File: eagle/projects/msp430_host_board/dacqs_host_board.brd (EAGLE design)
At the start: 127 x 100 mm, 271 parts, among them J1 MOL-SL-4-RA, J10 MOL-SL-3-V, J11 MOL-SL-2-V, J12 CONN HEADER 20POS .100" DBL, J13 MOL-SL-2-RA, J14 USB_MICROB_RECPT, J16 MOL-SL-2-RA, J17 CLM-112-02-L-D-IMU-MOUNT_IMU, J18 MOLSL-7-RA, J19 CONN HEADER 20POS .100" DBL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

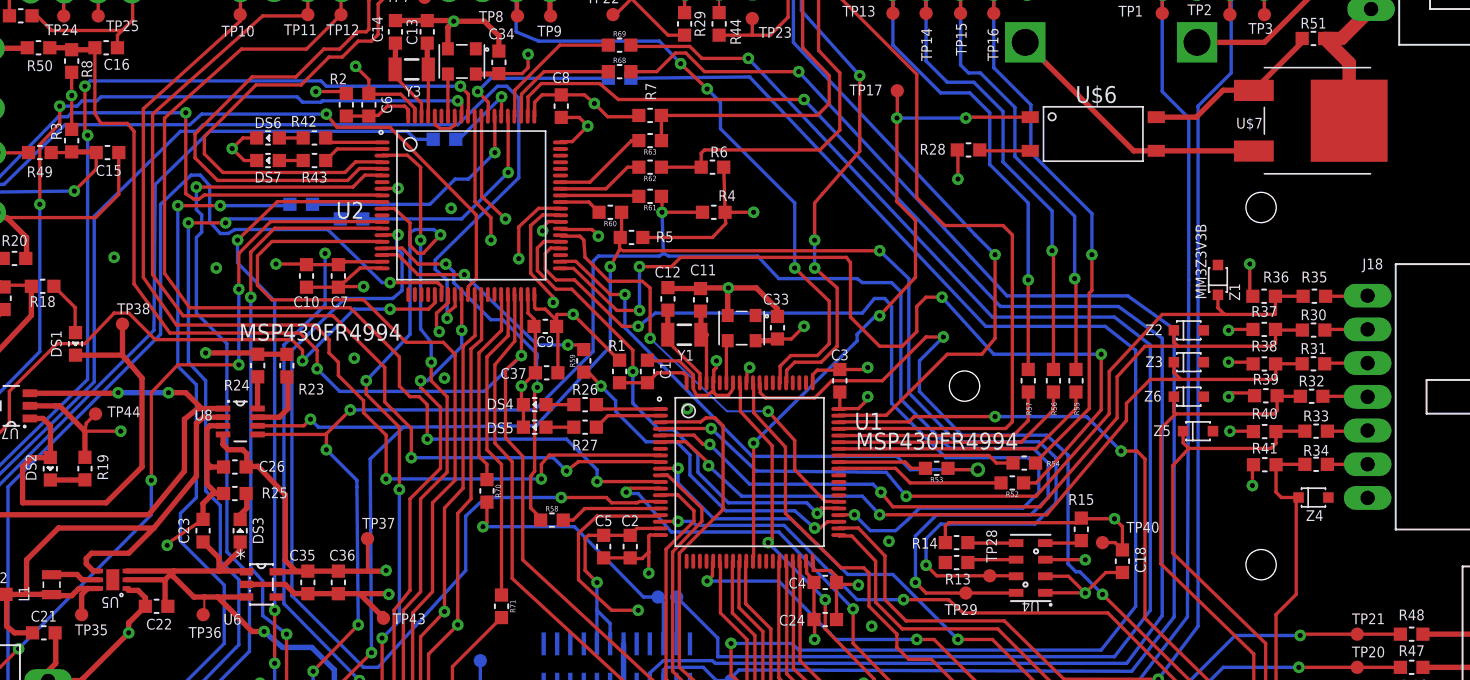
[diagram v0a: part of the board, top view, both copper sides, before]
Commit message: Small fixes to power packages and power fet layout
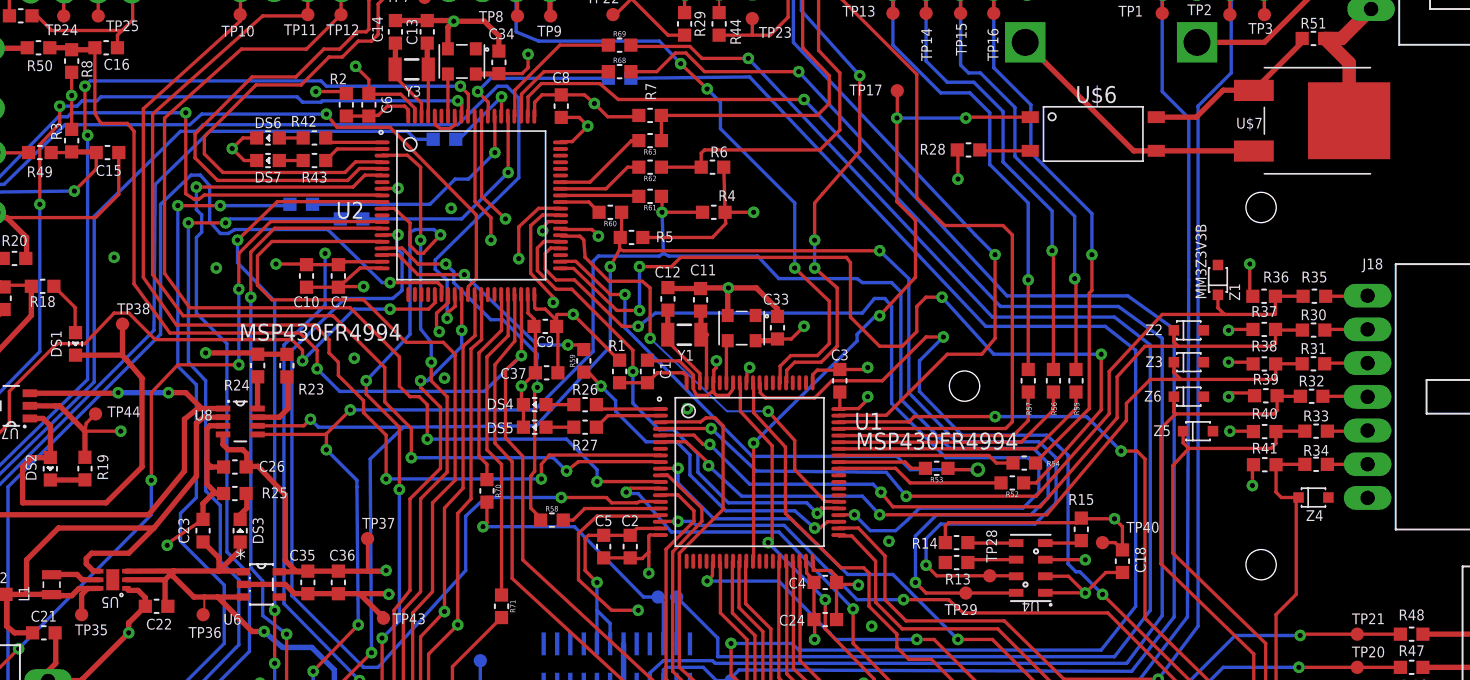
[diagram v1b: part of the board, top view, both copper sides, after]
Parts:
- R49, R50: value 47k -> 49.9
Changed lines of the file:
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@@
 <attribute name="VALUE" x="116.4" y="38.55" size="0.254" layer="27" ratio="6" rot="R180" align="center"/>
 </element>
-<element name="R49" library="daqcs_host" package="R0603" value="47k" x="13" y="74.1" smashed="yes">
-<attribute name="MANUFACTURER_PN" value="ERJ-3EKF4702V" x="13" y="74.1" size="1.778" layer="27" display="off"/>
+<element name="R49" library="daqcs_host" package="R0603" value="49.9" x="13" y="74.1" smashed="yes">
+<attribute name="MANUFACTURER_PN" value="ERJ-3EKF49R9V" x="13" y="74.1" size="1.778" layer="27" display="off"/>
 <attribute name="TOLERANCE" value="1%" x="13" y="74.1" size="1.778" layer="27" display="off"/>
-<attribute name="VENDOR_PN" value="P47.0KHCT-ND" x="13" y="74.1" size="1.778" layer="27" display="off"/>
+<attribute name="VENDOR_PN" value="P49.9HCT-ND" x="13" y="74.1" size="1.778" layer="27" display="off"/>
 <attribute name="MANUFACTURER" value="Panasonic" x="13" y="74.1" size="1.778" layer="27" display="off"/>
 <attribute name="POWER" value="1/10W" x="13" y="74.1" size="1.778" layer="27" display="off"/>
 <attribute name="VENDOR" value="Digi-key" x="13" y="74.1" size="1.778" layer="27" display="off"/>
 <attribute name="NAME" x="13" y="72.65" size="0.8128" layer="25" ratio="15" align="center"/>
-<attribute name="VALUE" x="13" y="73.35" size="0.254" layer="27" ratio="6" align="center"/>
+<attribute name="VALUE" value="49.9" x="13" y="73.35" size="0.254" layer="27" ratio="6" align="center"/>
 </element>
-<element name="R50" library="daqcs_host" package="R0603" value="47k" x="12.9" y="82" smashed="yes">
-<attribute name="MANUFACTURER_PN" value="ERJ-3EKF4702V" x="12.9" y="82" size="1.778" layer="27" display="off"/>
+<element name="R50" library="daqcs_host" package="R0603" value="49.9" x="12.9" y="82" smashed="yes">
+<attribute name="MANUFACTURER_PN" value="ERJ-3EKF49R9V" x="12.9" y="82" size="1.778" layer="27" display="off"/>
 <attribute name="TOLERANCE" value="1%" x="12.9" y="82" size="1.778" layer="27" display="off"/>
-<attribute name="VENDOR_PN" value="P47.0KHCT-ND" x="12.9" y="82" size="1.778" layer="27" display="off"/>
+<attribute name="VENDOR_PN" value="P49.9HCT-ND" x="12.9" y="82" size="1.778" layer="27" display="off"/>
 <attribute name="MANUFACTURER" value="Panasonic" x="12.9" y="82" size="1.778" layer="27" display="off"/>
 <attribute name="POWER" value="1/10W" x="12.9" y="82" size="1.778" layer="27" display="off"/>
 <attribute name="VENDOR" value="Digi-key" x="12.9" y="82" size="1.778" layer="27" display="off"/>
 <attribute name="NAME" x="13" y="80.65" size="0.8128" layer="25" ratio="15" align="center"/>
-<attribute name="VALUE" x="12.9" y="81.25" size="0.254" layer="27" ratio="6" align="center"/>
+<attribute name="VALUE" value="49.9" x="12.9" y="81.25" size="0.254" layer="27" ratio="6" align="center"/>
 </element>
 <element name="TP39" library="daqcs_host" package="TP10R" value="" x="32.4" y="21.2" smashed="yes">
@@
 <wire x1="31.5" y1="48.3" x2="31.5" y2="43.35" width="0.4064" layer="1"/>
 <wire x1="31.5" y1="43.35" x2="32.3" y2="42.55" width="0.4064" layer="1"/>
-<wire x1="30.8176" y1="42.5" x2="33.15" y2="42.5" width="0.4064" layer="1"/>
+<wire x1="31.05" y1="42.5" x2="33.15" y2="42.5" width="0.4064" layer="1"/>
 <wire x1="33.15" y1="42.5" x2="33.2" y2="42.55" width="0.4064" layer="1"/>
 <wire x1="37.7" y1="42.55" x2="39.05" y2="42.55" width="0.4064" layer="1"/>
@@
 <wire x1="38.9" y1="39.34290625" x2="38.60709375" y2="39.34290625" width="0.4064" layer="1"/>
 <wire x1="38.60709375" y1="39.34290625" x2="37.1" y2="40.85" width="0.4064" layer="1"/>
-<wire x1="28.5824" y1="41.55" x2="31.5" y2="41.55" width="0.4064" layer="1"/>
+<wire x1="28.35" y1="41.55" x2="31.5" y2="41.55" width="0.4064" layer="1"/>
 <wire x1="31.5" y1="41.55" x2="32.2" y2="40.85" width="0.4064" layer="1"/>
 <wire x1="14.2" y1="37.55" x2="14.15" y2="37.9" width="0.4064" layer="1"/>
@@
 <wire x1="20.95" y1="40.55" x2="20.4" y2="41.1" width="0.4064" layer="1"/>
 <wire x1="20.4" y1="41.1" x2="19.681" y2="41.1" width="0.4064" layer="1"/>
-<wire x1="19.681" y1="41.1" x2="19.5414" y2="41.2396" width="0.4064" layer="1"/>
+<wire x1="19.681" y1="41.1" x2="19.525" y2="41.25" width="0.4064" layer="1"/>
 <wire x1="26.85" y1="50.4" x2="25.9" y2="50.4" width="0.4064" layer="1"/>
 <wire x1="25.9" y1="50.4" x2="25.6" y2="50.7" width="0.4064" layer="1"/>
@@
 <wire x1="57.4" y1="32.2" x2="56.6" y2="32.2" width="0.4064" layer="16"/>
 <wire x1="56.998" y1="34.026" x2="56.998" y2="37.074" width="0.4064" layer="16"/>
-<wire x1="28.5824" y1="40.6" x2="26.4" y2="40.6" width="0.4064" layer="1"/>
+<wire x1="28.35" y1="40.6" x2="26.4" y2="40.6" width="0.4064" layer="1"/>
 <wire x1="26.4" y1="40.6" x2="25.4" y2="40.6" width="0.4064" layer="1"/>
 <wire x1="25.4" y1="40.6" x2="24.60975625" y2="40.6" width="0.4064" layer="1"/>
@@
 <wire x1="29.9" y1="38" x2="29" y2="38" width="0.4064" layer="1"/>
 <wire x1="29" y1="38" x2="26.4" y2="40.6" width="0.4064" layer="1"/>
-<wire x1="19.5414" y1="42.5604" x2="23.1" y2="42.5604" width="0.4064" layer="1"/>
+<wire x1="19.525" y1="42.55" x2="23.1" y2="42.5604" width="0.4064" layer="1"/>
 <wire x1="23.1" y1="42.5604" x2="26.5" y2="42.5604" width="0.4064" layer="1"/>
 <wire x1="26.5" y1="42.5604" x2="28.522" y2="42.5604" width="0.4064" layer="1"/>
-<wire x1="28.522" y1="42.5604" x2="28.5824" y2="42.5" width="0.4064" layer="1"/>
-<wire x1="19.5414" y1="41.9" x2="22.4396" y2="41.9" width="0.4064" layer="1"/>
+<wire x1="28.522" y1="42.5604" x2="28.35" y2="42.5" width="0.4064" layer="1"/>
+<wire x1="19.525" y1="41.9" x2="22.4396" y2="41.9" width="0.4064" layer="1"/>
 <wire x1="22.4396" y1="41.9" x2="22.8698" y2="42.3302" width="0.4064" layer="1"/>
 <wire x1="22.8698" y1="42.3302" x2="23.1" y2="42.5604" width="0.4064" layer="1"/>
@@
 <contactref element="U5" pad="5"/>
 <contactref element="L1" pad="2"/>
-<wire x1="17.4586" y1="41.9" x2="16.2" y2="41.9" width="0.4064" layer="1"/>
+<wire x1="17.475" y1="41.9" x2="16.2" y2="41.9" width="0.4064" layer="1"/>
 <wire x1="16.2" y1="41.9" x2="15.8" y2="42.3" width="0.4064" layer="1"/>
 <wire x1="15.8" y1="42.3" x2="13.91" y2="42.3" width="0.4064" layer="1"/>
@@
 <wire x1="12" y1="43.4" x2="12" y2="40.9" width="0.4064" layer="1"/>
 <wire x1="12" y1="40.9" x2="11.9" y2="40.8" width="0.4064" layer="1"/>
-<wire x1="17.4586" y1="42.5604" x2="17.0396" y2="42.5604" width="0.4064" layer="1"/>
+<wire x1="17.475" y1="42.55" x2="17.0396" y2="42.5604" width="0.4064" layer="1"/>
 <wire x1="17.0396" y1="42.5604" x2="16.5" y2="43.1" width="0.4064" layer="1"/>
 <wire x1="16.5" y1="43.1" x2="16.5" y2="43.5" width="0.4064" layer="1"/>
 <wire x1="16.5" y1="43.5" x2="16.9" y2="43.9" width="0.4064" layer="1"/>
 <wire x1="16.9" y1="43.9" x2="19.7" y2="43.9" width="0.4064" layer="1"/>
-<wire x1="17.4586" y1="41.2396" x2="16.6" y2="41.2396" width="0.4064" layer="1"/>
+<wire x1="17.475" y1="41.25" x2="16.6" y2="41.2396" width="0.4064" layer="1"/>
 <wire x1="16.6" y1="41.2396" x2="15.9396" y2="41.2396" width="0.4064" layer="1"/>
 <wire x1="15.9396" y1="41.2396" x2="15.4" y2="40.7" width="0.4064" layer="1"/>

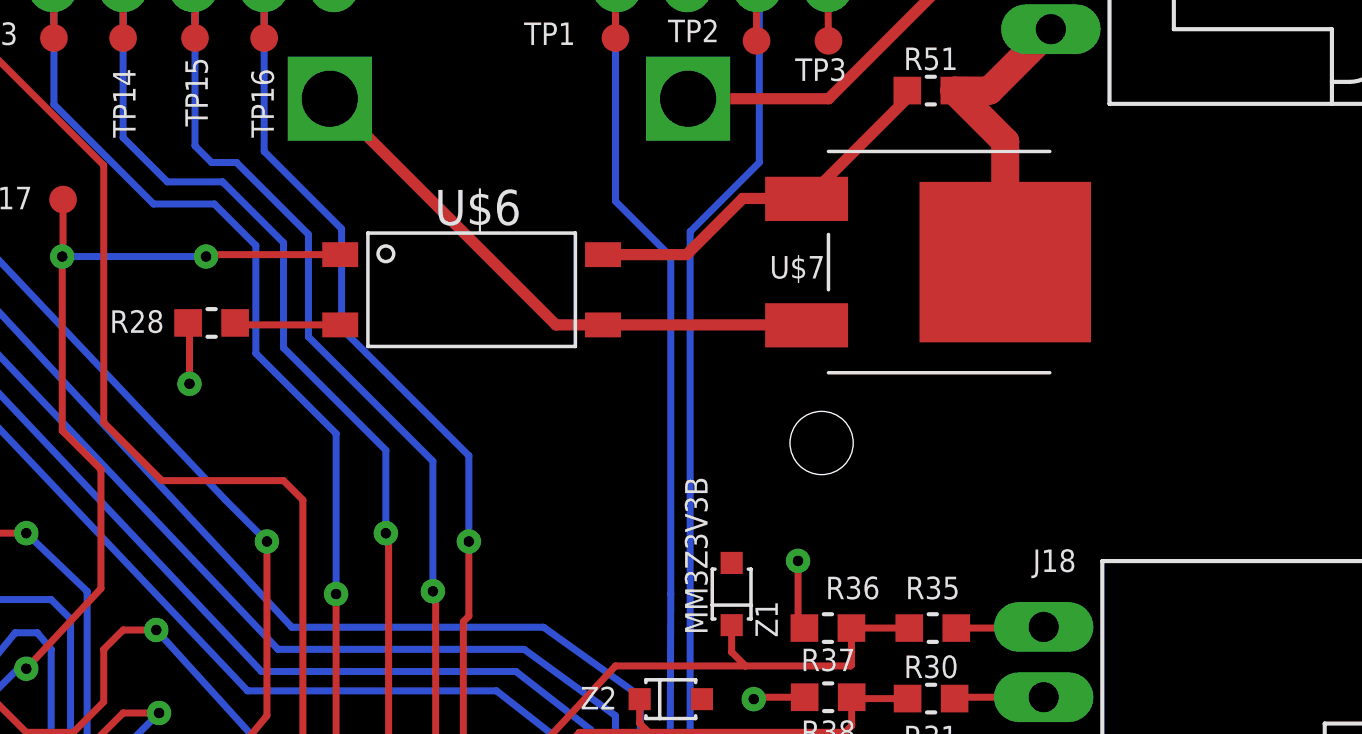
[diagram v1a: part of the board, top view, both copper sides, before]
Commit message: Updated R28 to 2k, updated all voltage dividers such that internal 2.5V on MSP430 can be used, added a pull down resistor for the cutdown_en signal incase of power glitches at powerup
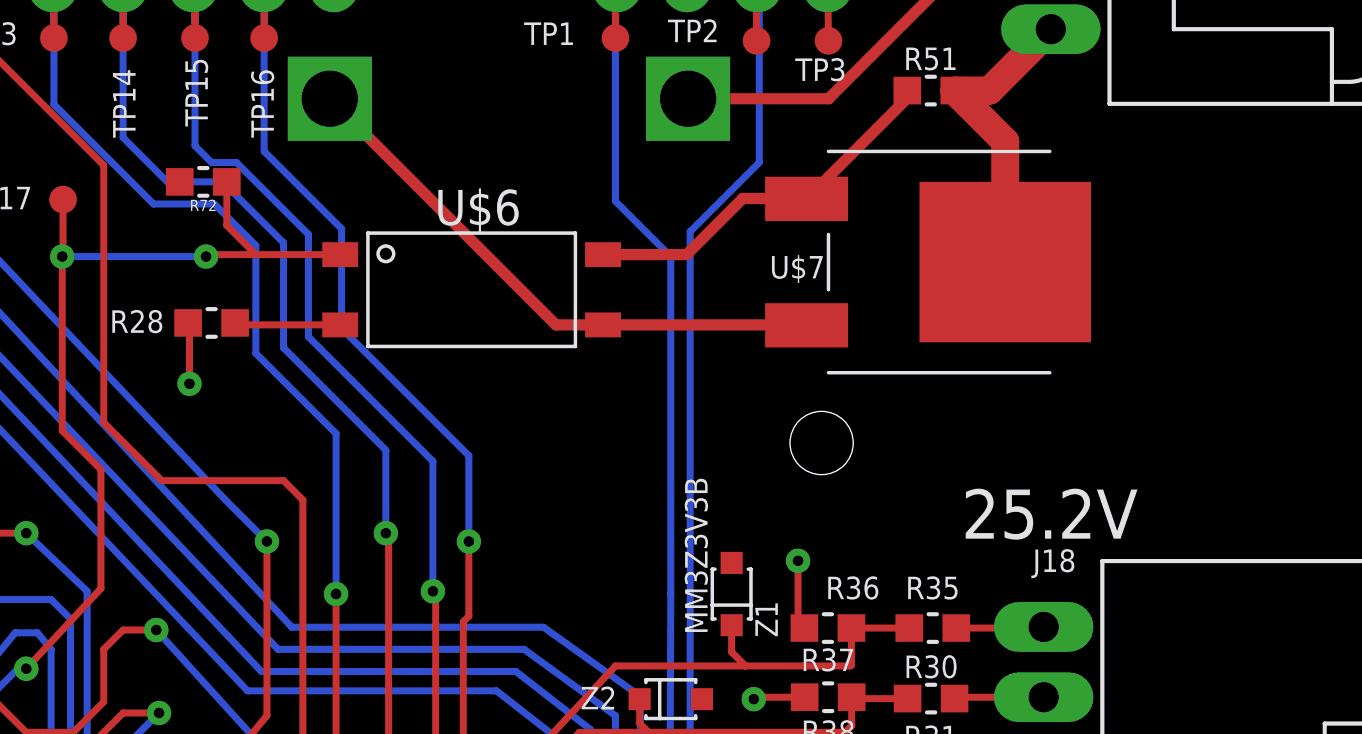
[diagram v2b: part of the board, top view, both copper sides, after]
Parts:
- added R72: 49.9k, daqcs_host:R0603
- R28: value 49.9k -> 2k
- R30: value 60.4k -> 10.2k
- R31: value 69.8k -> 10.7k
- R32: value 49.9k -> 4.12k
- R33: value 49.9k -> 10.2k
- R34: value 12k -> 1.02k
- R35: value 49.9k -> 68.1k
- R36: value 7.15k -> 7.5k
- R37: value 10k -> 1.37k
- R38: value 15k -> 1.87k
- R39: value 15k -> 1.02k
- R40: value 30k -> 4.32k
- R41: value 30k -> 1.5k
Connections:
- net CUTDOWN_EN: now also R72.1
- net GND: now also R72.2
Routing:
- net CUTDOWN_EN: track 51.3 -> 54.4 mm
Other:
- board text added: "25.2V"
